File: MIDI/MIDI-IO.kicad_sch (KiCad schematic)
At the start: 17 parts

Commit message: Fix missong symbols
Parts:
- removed D?: DUS, symbol Device:D_Small_ALT
- removed D?: LED3MM, symbol Device:LED_Small_ALT
- added D?: MIDI-IN, symbol Device:LED_Small_Filled
- added D?: DUS, symbol Device:D_Small_Filled
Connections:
- net +5V: now also D?.2 (A)
- net at J?.5, U?.3: now also D?.2 (A)
- net at R?.2, U?.2: now also D?.1 (K)
- net at Q?.1 (C): now also D?.1 (K)
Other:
- note removed: "SIGNAL-IN"
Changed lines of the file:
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@@
   (junction (at 189.23 83.82) (diameter 0) (color 0 0 0 0)
   )
+  (junction (at 214.63 86.36) (diameter 0) (color 0 0 0 0)
+  )
   (junction (at 194.31 93.98) (diameter 0) (color 0 0 0 0)
+  )
+  (junction (at 214.63 91.44) (diameter 0) (color 0 0 0 0)
   )
   (no_connect (at 241.3 55.88))
@@
   (no_connect (at 242.57 109.22))
   (no_connect (at 226.06 83.82))
-  (wire (pts (xy 212.09 86.36) (xy 218.44 86.36))
+  (wire (pts (xy 214.63 86.36) (xy 218.44 86.36))
+    (stroke (width 0) (type default) (color 0 0 0 0))
+  )
+  (wire (pts (xy 212.09 86.36) (xy 214.63 86.36))
     (stroke (width 0) (type default) (color 0 0 0 0))
   )
@@
     (stroke (width 0) (type default) (color 0 0 0 0))
   )
+  (wire (pts (xy 214.63 91.44) (xy 228.6 91.44))
+    (stroke (width 0) (type default) (color 0 0 0 0))
+  )
   (wire (pts (xy 237.49 132.08) (xy 237.49 133.35))
     (stroke (width 0) (type default) (color 0 0 0 0))
@@
     (stroke (width 0) (type default) (color 0 0 0 0))
   )
-  (wire (pts (xy 212.09 91.44) (xy 228.6 91.44))
+  (wire (pts (xy 212.09 91.44) (xy 214.63 91.44))
     (stroke (width 0) (type default) (color 0 0 0 0))
   )
@@
   (wire (pts (xy 182.88 58.42) (xy 218.44 58.42))
     (stroke (width 0) (type default) (color 0 0 0 0))
-  )
-  (text "SIGNAL-IN" (at 240.03 138.43 0)
-    (effects (font (size 1.524 1.524)) (justify left bottom))
   )
   (label "TXD" (at 182.88 58.42 0)
@@
     )
     (pin "1")
-  )
-  (symbol (lib_id "Device:D_Small_ALT") (at 214.63 88.9 270) (unit 1)
-    (in_bom yes) (on_board yes)
-    (property "Reference" "D?" (id 0) (at 216.3572 87.8586 90)
-      (effects (font (size 1.27 1.27)) (justify left))
-    )
-    (property "Value" "DUS" (id 1) (at 216.3572 90.0684 90)
-      (effects (font (size 1.1176 1.1176)) (justify left))
-    )
-    (property "Footprint" "" (id 2) (at 214.63 88.9 90)
-      (effects (font (size 1.27 1.27)) hide)
-    )
-    (property "Datasheet" "~" (id 3) (at 214.63 88.9 90)
-      (effects (font (size 1.27 1.27)) hide)
-    )
   )
   (symbol (lib_id "Device:R_Small") (at 220.98 111.76 270) (unit 1)
@@
     (pin "3")
   )
-  (symbol (lib_id "Device:LED_Small_ALT") (at 237.49 135.89 90) (unit 1)
-    (in_bom yes) (on_board yes)
-    (property "Reference" "D?" (id 0) (at 232.41 134.62 90)
-      (effects (font (size 1.27 1.27)) (justify right))
-    )
-    (property "Value" "LED3MM" (id 1) (at 228.6 138.43 90)
-      (effects (font (size 1.27 1.27)) (justify right))
-    )
-    (property "Footprint" "" (id 2) (at 237.49 135.89 90)
-      (effects (font (size 1.27 1.27)) hide)
-    )
-    (property "Datasheet" "~" (id 3) (at 237.49 135.89 90)
-      (effects (font (size 1.27 1.27)) hide)
-    )
-  )
   (symbol (lib_id "Connector:DIN-5_180degree") (at 234.95 109.22 180) (unit 1)
     (in_bom yes) (on_board yes)
@@
     (pin "5")
   )
+  (symbol (lib_id "Device:LED_Small_Filled") (at 237.49 135.89 90) (unit 1)
+    (in_bom yes) (on_board yes) (fields_autoplaced)
+    (property "Reference" "D?" (id 0) (at 239.268 134.9918 90)
+      (effects (font (size 1.27 1.27)) (justify right))
+    )
+    (property "Value" "MIDI-IN" (id 1) (at 239.268 137.5287 90)
+      (effects (font (size 1.27 1.27)) (justify right))
+    )
+    (property "Footprint" "" (id 2) (at 237.49 135.89 90)
+      (effects (font (size 1.27 1.27)) hide)
+    )
+    (property "Datasheet" "~" (id 3) (at 237.49 135.89 90)
+      (effects (font (size 1.27 1.27)) hide)
+    )
+    (pin "1")
+    (pin "2")
+  )
+  (symbol (lib_id "Device:D_Small_Filled") (at 214.63 88.9 270) (unit 1)
+    (in_bom yes) (on_board yes) (fields_autoplaced)
+    (property "Reference" "D?" (id 0) (at 216.408 88.1601 90)
+      (effects (font (size 1.27 1.27)) (justify left))
+    )
+    (property "Value" "DUS" (id 1) (at 216.408 90.5442 90)
+      (effects (font (size 1.1 1.1)) (justify left))
+    )
+    (property "Footprint" "" (id 2) (at 214.63 88.9 90)
+      (effects (font (size 1.27 1.27)) hide)
+    )
+    (property "Datasheet" "~" (id 3) (at 214.63 88.9 90)
+      (effects (font (size 1.27 1.27)) hide)
+    )
+    (pin "1")
+    (pin "2")
+  )
   (sheet_instances
     (path "/" (page "1"))
@@
       (reference "#PWR?") (unit 1) (value "+5V") (footprint "")
     )
-    (path "/00000000-0000-0000-0000-00005b798b29"
+    (path "/85718ecc-58f1-4a33-8af4-a21e6cb24cfe"
+      (reference "D?") (unit 1) (value "MIDI-IN") (footprint "")
+    )
+    (path "/ce2b4044-8a57-4283-9bab-fe85def8b064"
       (reference "D?") (unit 1) (value "DUS") (footprint "")
     )
-    (path "/00000000-0000-0000-0000-00005b79b9f7"
-      (reference "D?") (unit 1) (value "LED3MM") (footprint "")
-    )
     (path "/00000000-0000-0000-0000-00005b797d35"

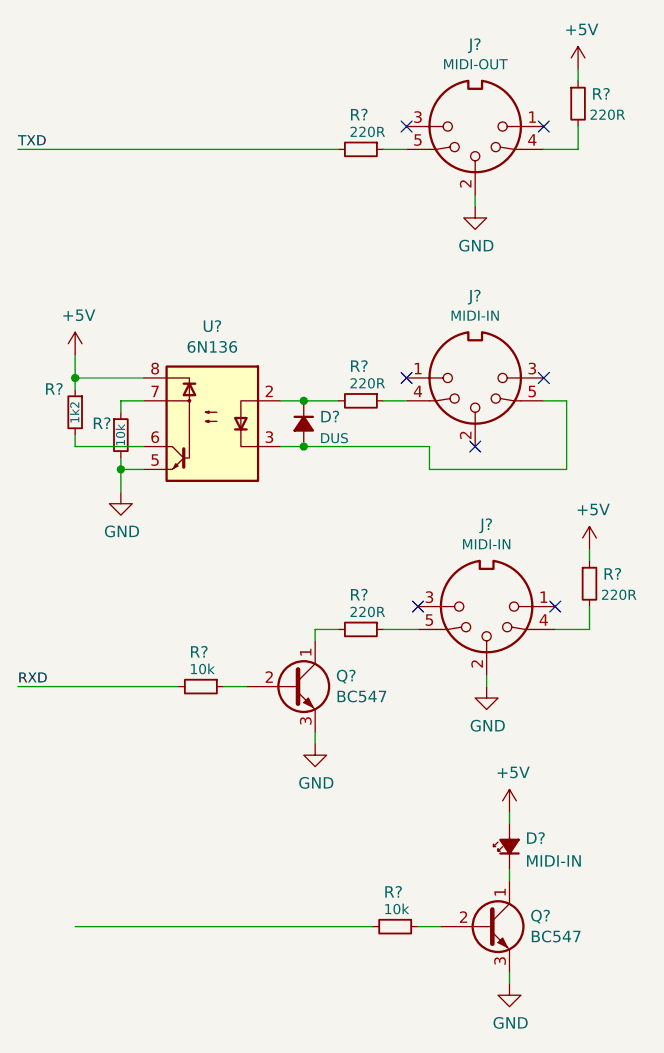
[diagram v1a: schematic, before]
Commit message: Fix grid alignment and update to KiCad 9
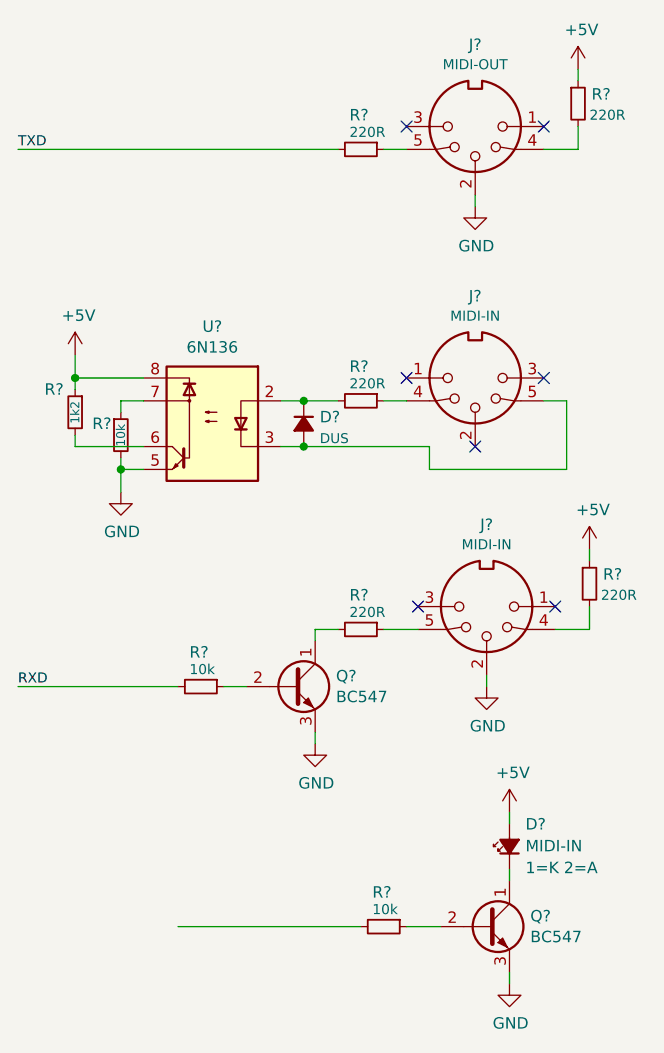
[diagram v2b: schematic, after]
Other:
- moved on the sheet: R?

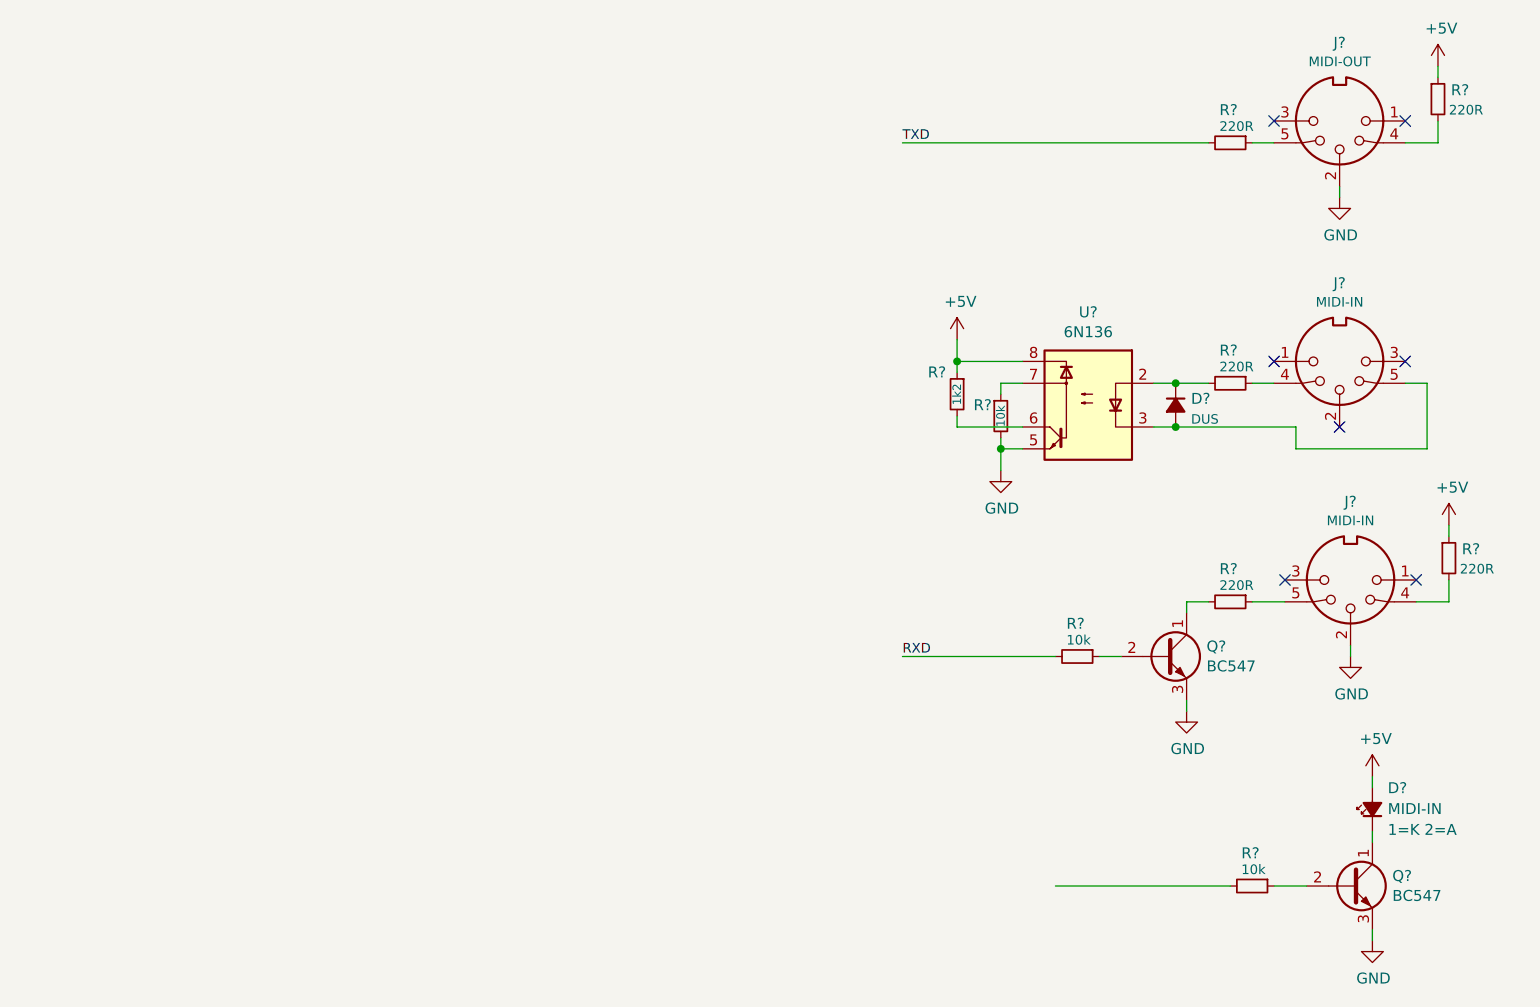
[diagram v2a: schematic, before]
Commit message: Add H11L1 to MIDI I/O board
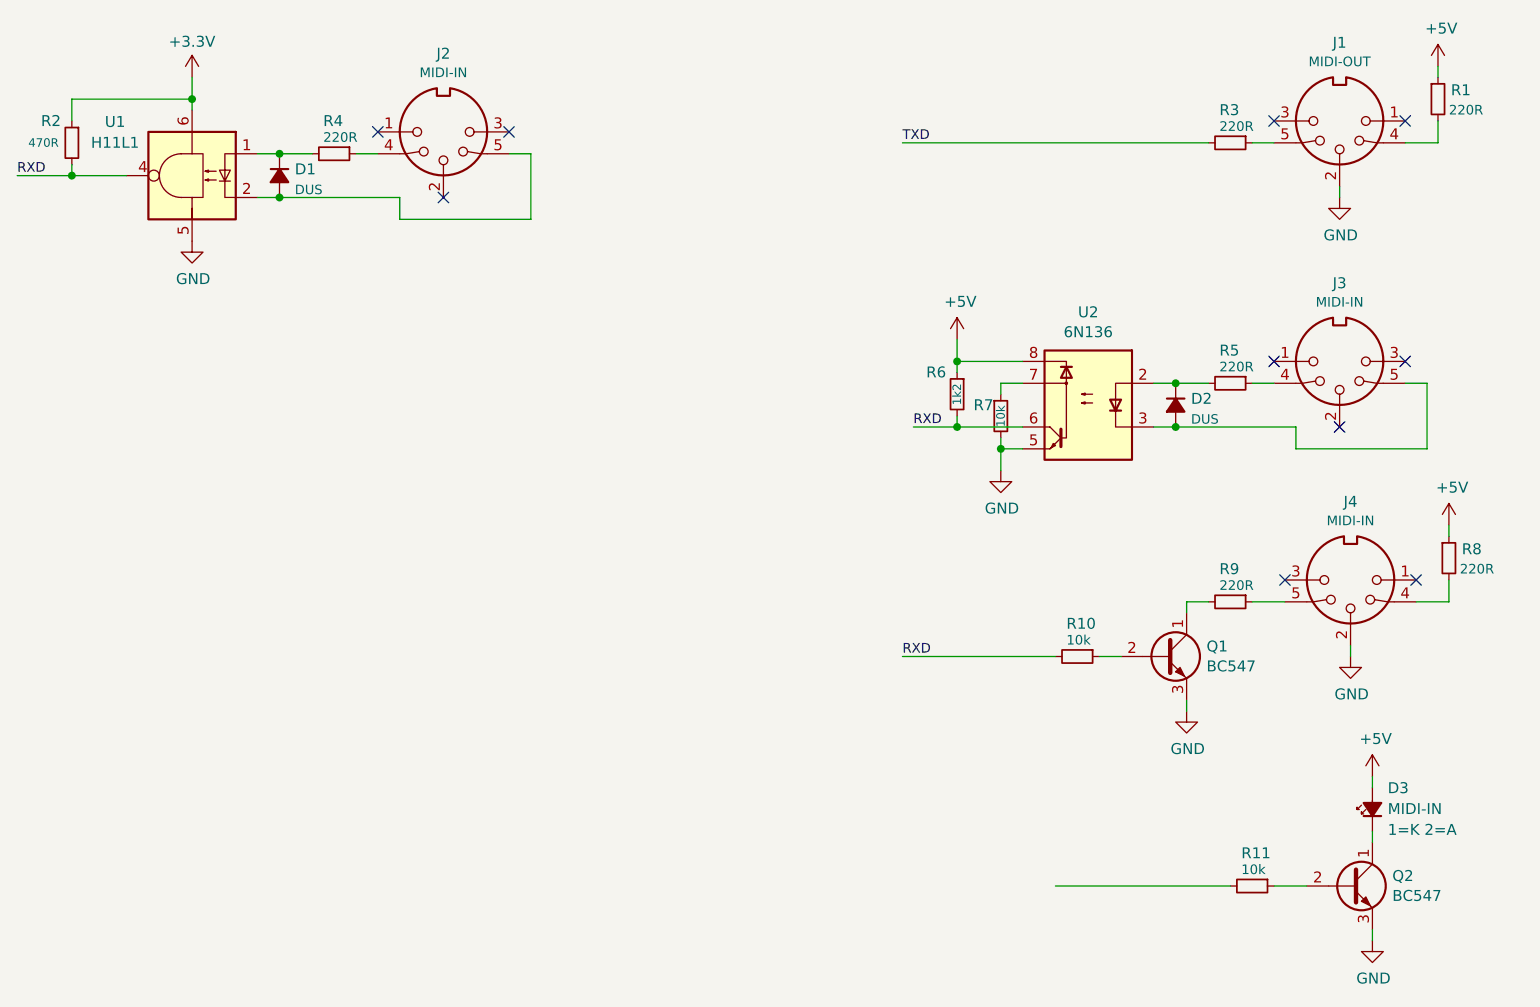
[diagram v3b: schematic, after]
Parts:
- added D1: DUS, symbol Device:D_Small_Filled
- added J2: MIDI-IN, symbol Connector:DIN-5_180degree
- added R2: 470R, symbol Device:R_Small
- added R4: 220R, symbol Device:R_Small
- added U1: H11L1, Package_DIP:DIP-6_W7.62mm_Socket_LongPads, symbol Isolator:H11L1
- gave numbers to parts that had none: 17
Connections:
- net GND: now also U1.5
- net RXD: now also R6.2, U2.6, R2.2, U1.4
- new net: J2.4, R4.1
- new net: D1.2 (A), J2.5, U1.2
- new net: D1.1 (K), R4.2, U1.1
- new net +3.3V: R2.1, U1.6
- no-connect marks 7 -> 10
